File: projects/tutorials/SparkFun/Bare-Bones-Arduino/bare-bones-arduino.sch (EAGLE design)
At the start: 15 parts, among them J1 POWER_JACK, J2 AVR_SPI_PROG_3X2PTH, U1 328P

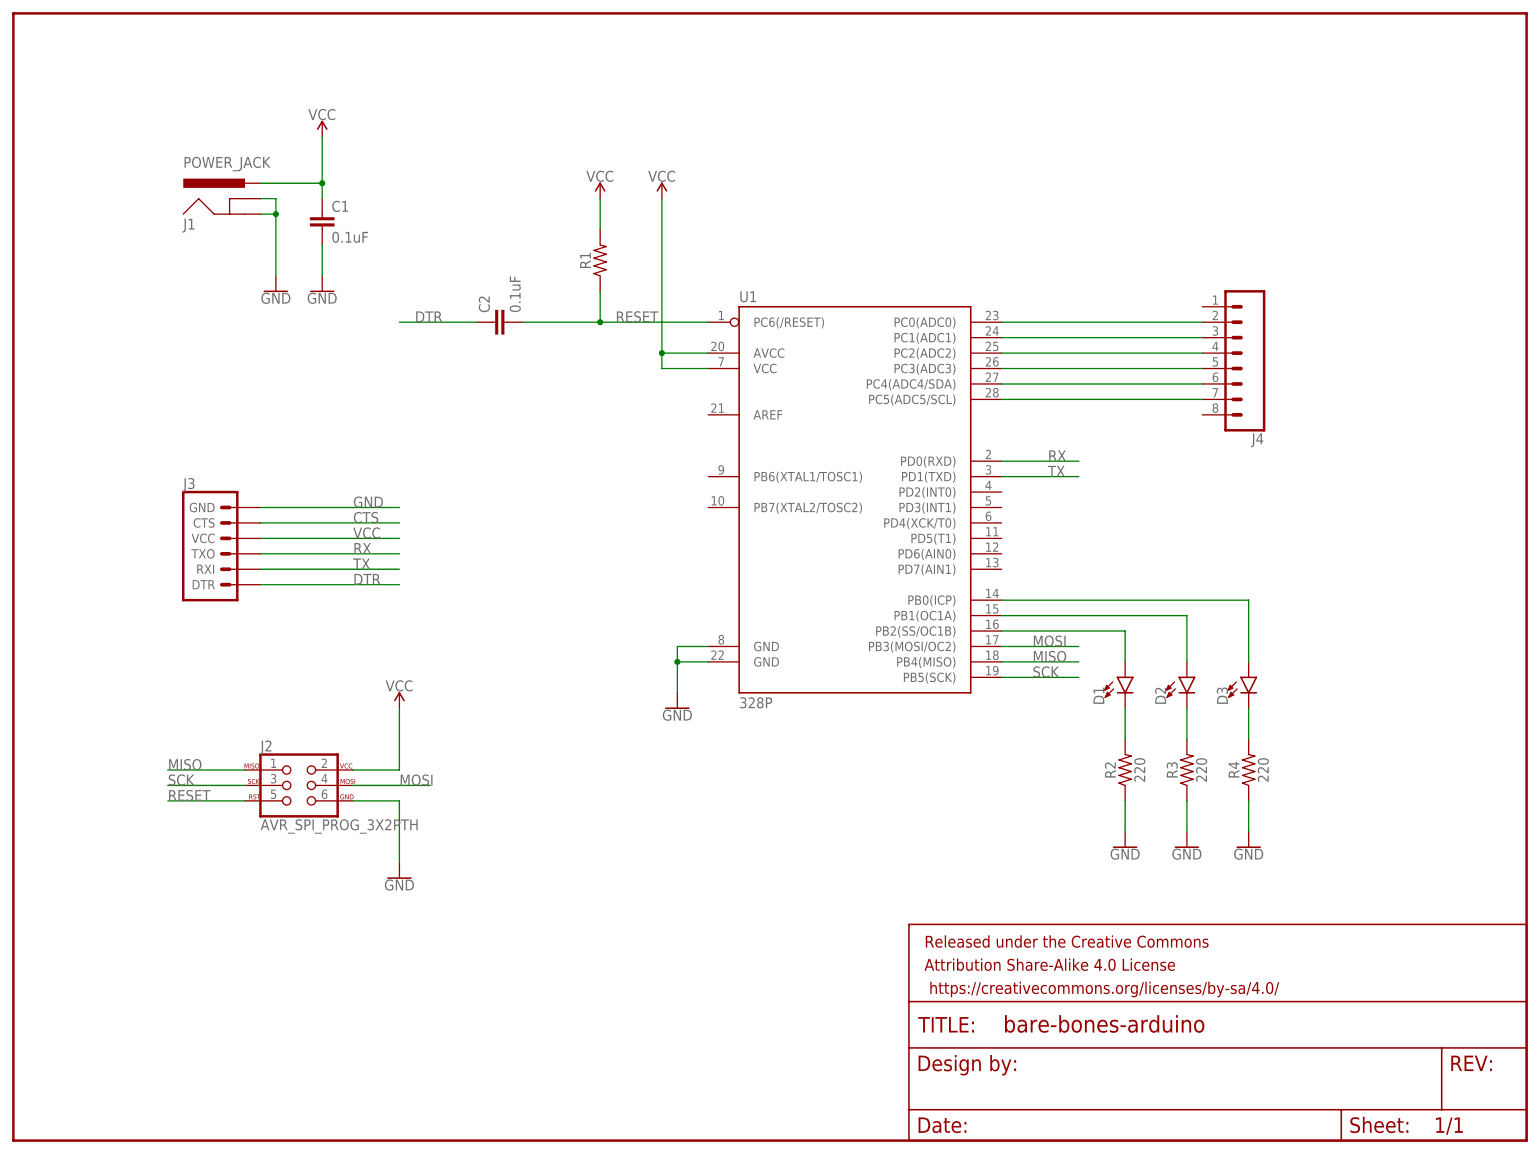
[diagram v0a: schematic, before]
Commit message: Added values to headers to get rid of warnings
Signed-off-by: Naveed Kawsar <naveedkawsar@outlook.com>
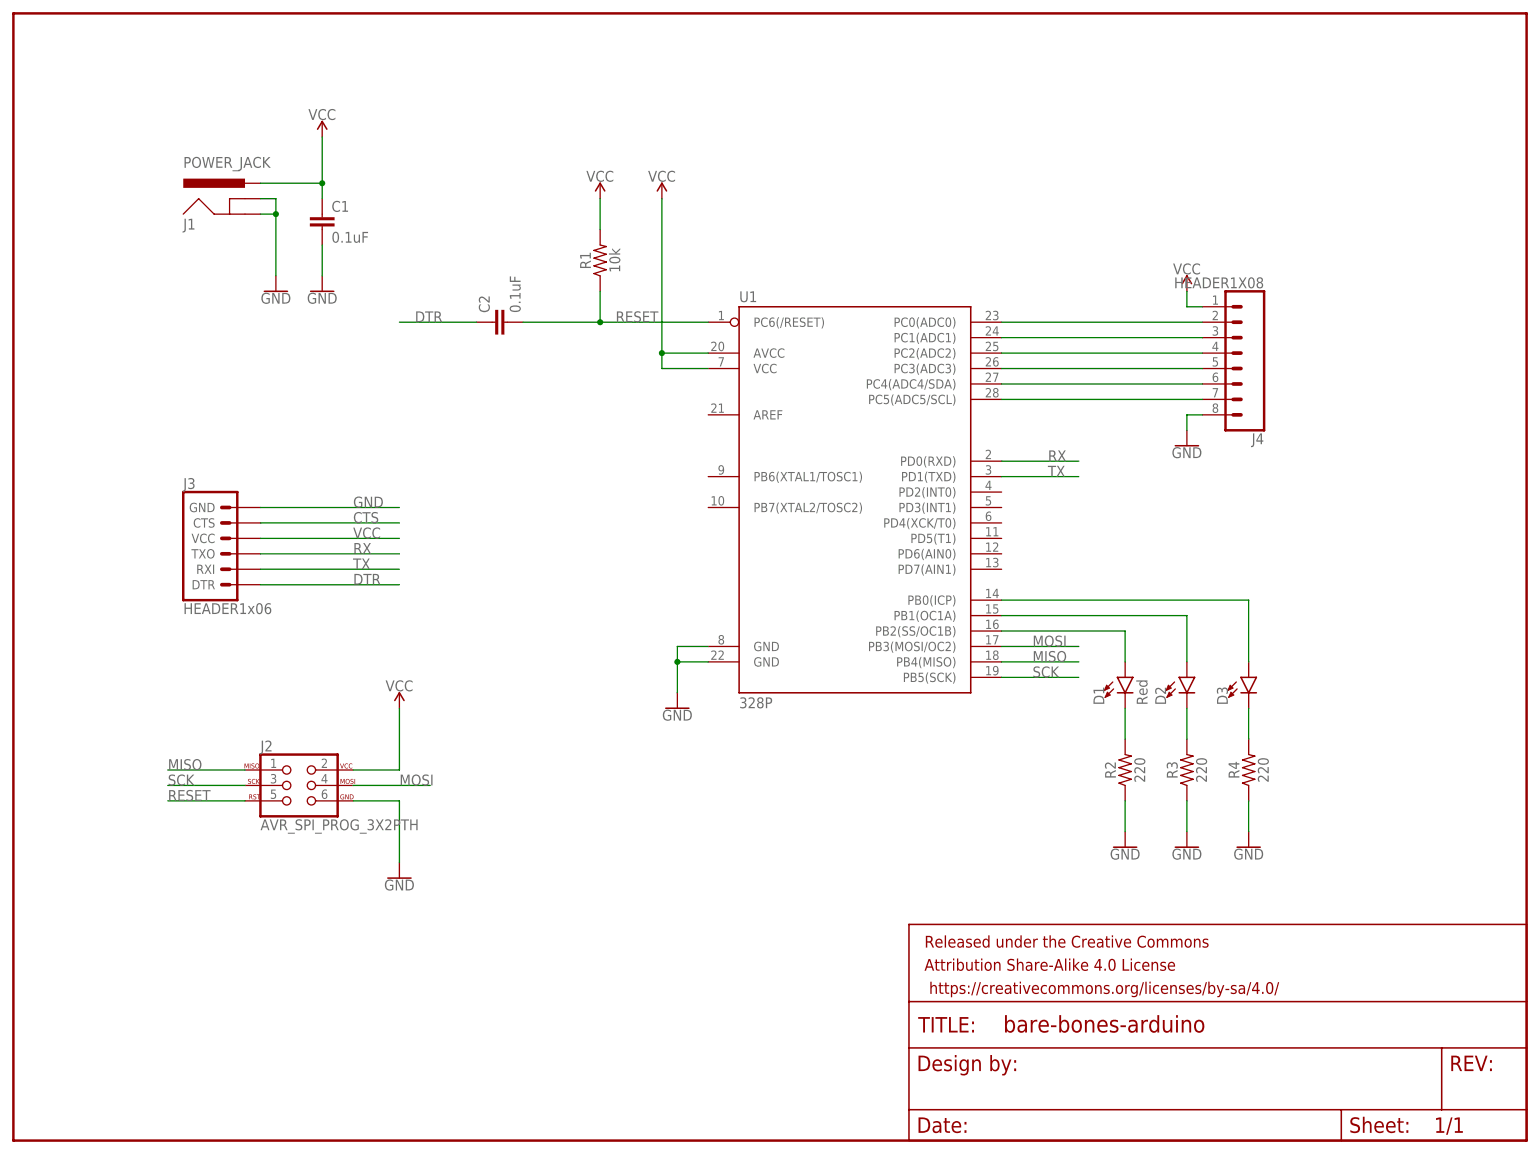
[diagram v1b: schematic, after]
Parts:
- D1: value (none) -> Red
- J3: value (none) -> HEADER1x06
- J4: value (none) -> HEADER1X08
- R1: value (none) -> 10k
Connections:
- net GND: now also J4.8
- net VCC: now also J4.1
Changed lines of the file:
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@@
 <part name="GND2" library="SparkFun-PowerSymbols" deviceset="GND" device=""/>
 <part name="U1" library="SparkFun-IC-Microcontroller" deviceset="ATMEGA328P_PDIP" device="" value="328P"/>
-<part name="D1" library="SparkFun-LED" deviceset="LED" device="5MM"/>
+<part name="D1" library="SparkFun-LED" deviceset="LED" device="5MM" value="Red"/>
 <part name="D2" library="SparkFun-LED" deviceset="LED" device="5MM"/>
 <part name="D3" library="SparkFun-LED" deviceset="LED" device="5MM"/>
 <part name="SUPPLY2" library="SparkFun-PowerSymbols" deviceset="VCC" device=""/>
 <part name="SUPPLY3" library="SparkFun-PowerSymbols" deviceset="VCC" device=""/>
-<part name="R1" library="SparkFun-Resistors" deviceset="RESISTOR" device="AXIAL-0.3" value=" "/>
+<part name="R1" library="SparkFun-Resistors" deviceset="RESISTOR" device="AXIAL-0.3" value=" 10k"/>
 <part name="R2" library="SparkFun-Resistors" deviceset="RESISTOR" device="AXIAL-0.3" value=" 220"/>
 <part name="R3" library="SparkFun-Resistors" deviceset="RESISTOR" device="AXIAL-0.3" value=" 220"/>
@@
 <part name="C2" library="SparkFun-Capacitors" deviceset="0.1UF" device="-KIT-EZ-50V-20%" value="0.1uF"/>
 <part name="J2" library="SparkFun-Connectors" deviceset="AVR_SPI_PROG_3X2" device="PTH"/>
-<part name="J3" library="SparkFun-Connectors" deviceset="6_PIN_SERIAL_TARGET" device=""/>
-<part name="J4" library="SparkFun-Connectors" deviceset="CONN_08" device="&quot;"/>
+<part name="J3" library="SparkFun-Connectors" deviceset="6_PIN_SERIAL_TARGET" device="" value="HEADER1x06"/>
+<part name="J4" library="SparkFun-Connectors" deviceset="CONN_08" device="&quot;" value="HEADER1X08"/>
 <part name="SUPPLY4" library="SparkFun-PowerSymbols" deviceset="VCC" device=""/>
 <part name="GND7" library="SparkFun-PowerSymbols" deviceset="GND" device=""/>
+<part name="GND8" library="SparkFun-PowerSymbols" deviceset="GND" device=""/>
+<part name="SUPPLY5" library="SparkFun-PowerSymbols" deviceset="VCC" device=""/>
 </parts>
 <sheets>
@@
 <instance part="SUPPLY4" gate="G$1" x="63.5" y="71.12"/>
 <instance part="GND7" gate="1" x="63.5" y="43.18"/>
+<instance part="GND8" gate="1" x="193.04" y="114.3"/>
+<instance part="SUPPLY5" gate="G$1" x="193.04" y="139.7"/>
 </instances>
 <busses>
@@
 <wire x1="63.5" y1="55.88" x2="63.5" y2="45.72" width="0.1524" layer="91"/>
 </segment>
+<segment>
+<pinref part="GND8" gate="1" pin="GND"/>
+<wire x1="193.04" y1="116.84" x2="193.04" y2="119.38" width="0.1524" layer="91"/>
+<pinref part="J4" gate="G$1" pin="8"/>
+<wire x1="193.04" y1="119.38" x2="195.58" y2="119.38" width="0.1524" layer="91"/>
+</segment>
 </net>
 <net name="VCC" class="0">
@@
 <wire x1="63.5" y1="60.96" x2="63.5" y2="71.12" width="0.1524" layer="91"/>
 </segment>
+<segment>
+<pinref part="J4" gate="G$1" pin="1"/>
+<wire x1="195.58" y1="137.16" x2="193.04" y2="137.16" width="0.1524" layer="91"/>
+<pinref part="SUPPLY5" gate="G$1" pin="VCC"/>
+<wire x1="193.04" y1="137.16" x2="193.04" y2="139.7" width="0.1524" layer="91"/>
+</segment>
 </net>

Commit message: Updated barebones Arduino schematic with parts named
Signed-off-by: Naveed Kawsar <naveedkawsar@outlook.com>
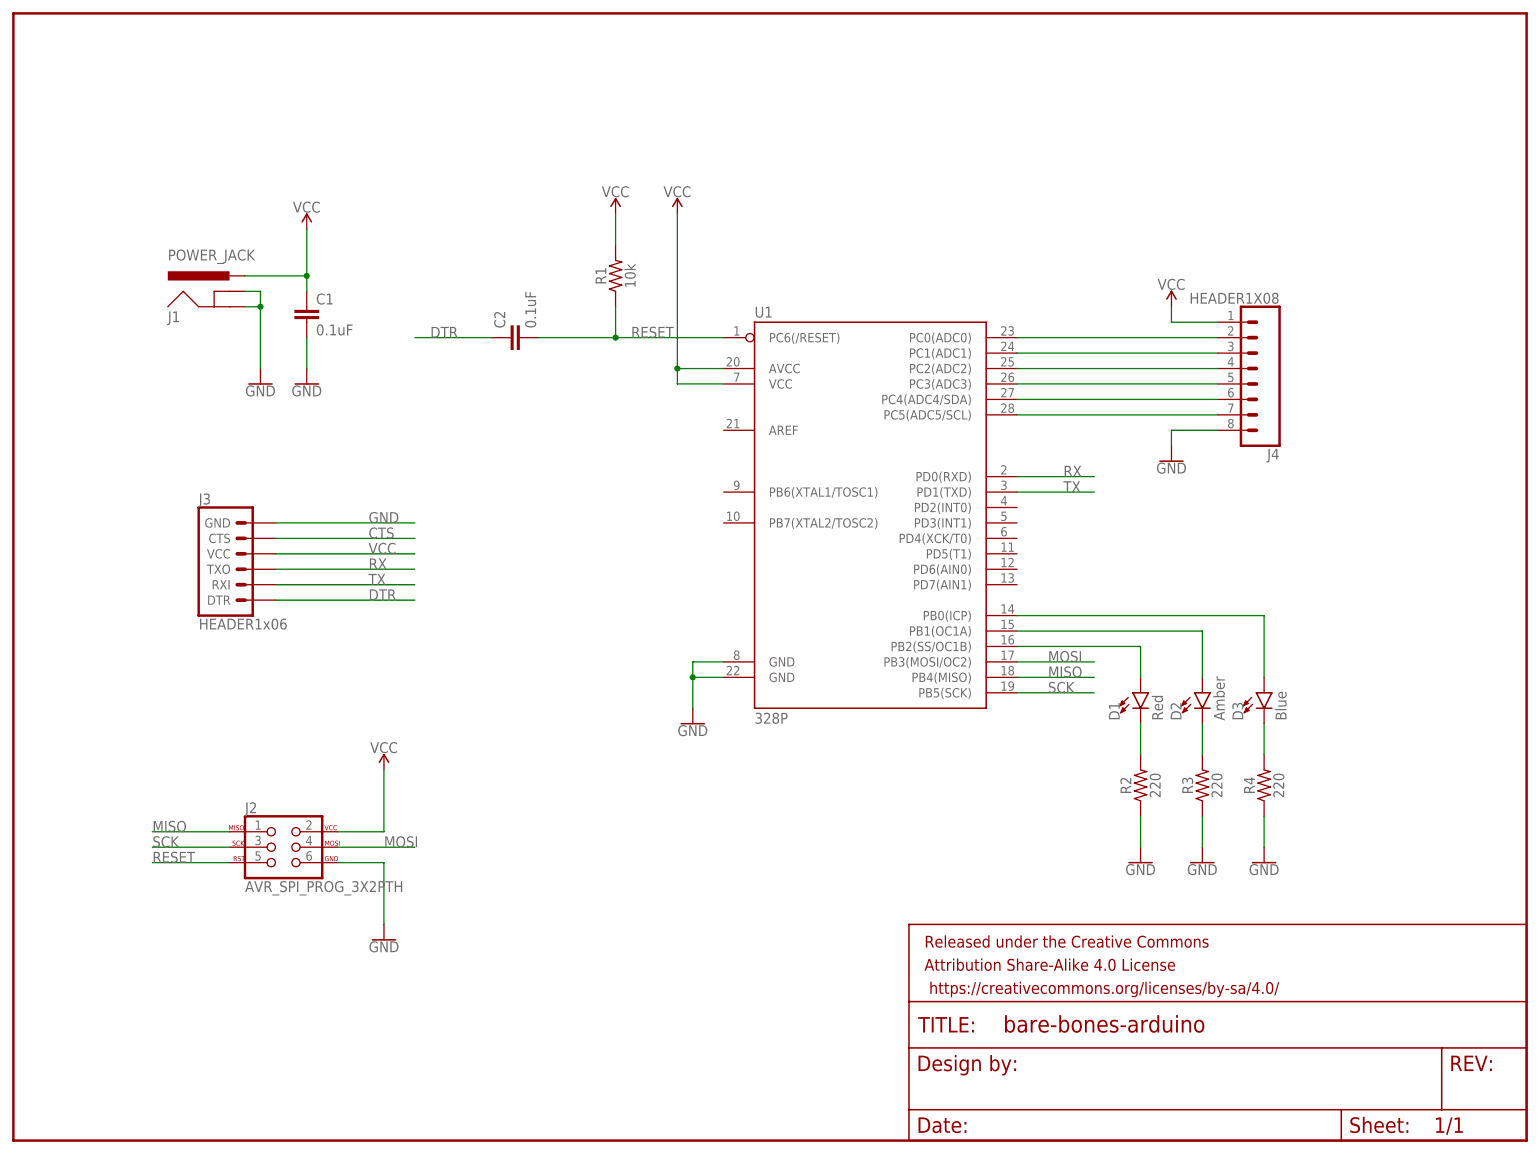
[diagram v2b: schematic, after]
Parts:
- D2: value (none) -> Amber
- D3: value (none) -> Blue
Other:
- moved on the sheet: C1, C2, D1, D2, D3, J1, J2, J3, J4, R1, R2, R3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
